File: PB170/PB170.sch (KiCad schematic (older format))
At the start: 47 parts, among them J2 USB_B_Micro, Q1 P-MOSFET-MLP_HS, SW1 SW_MEC_5E, SW2 SW_MEC_5E, U1 74HC00, U10 74HC74, U11 74HC74, U12 74HC74, U13 74HC74, U14 NE555DR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

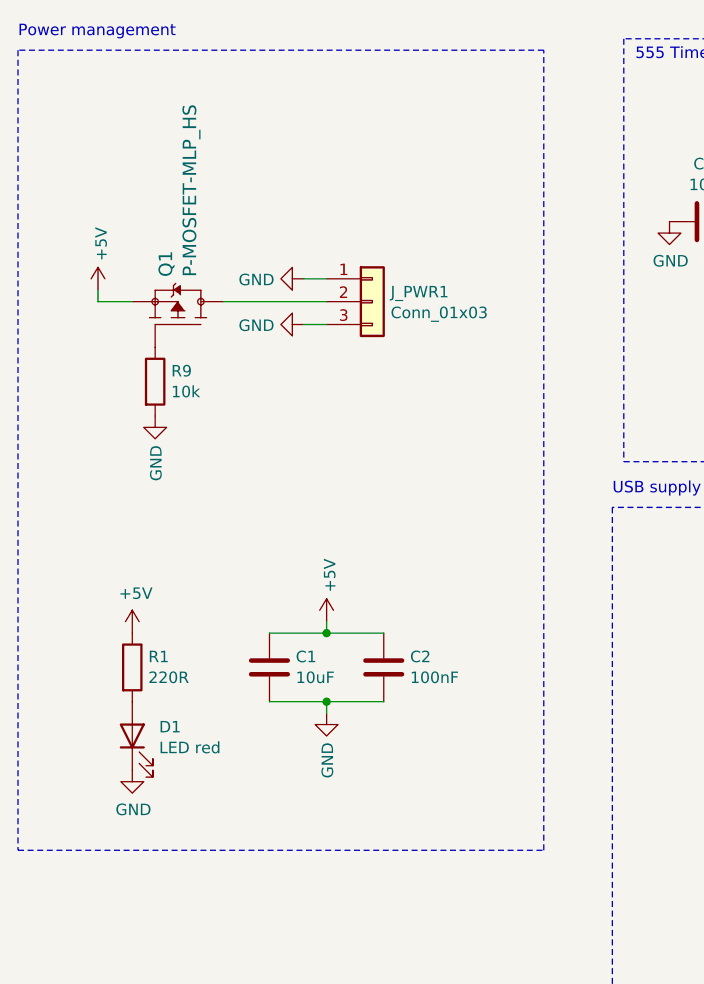
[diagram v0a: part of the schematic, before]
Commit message: Capacitors footprints added, gl & hf routing
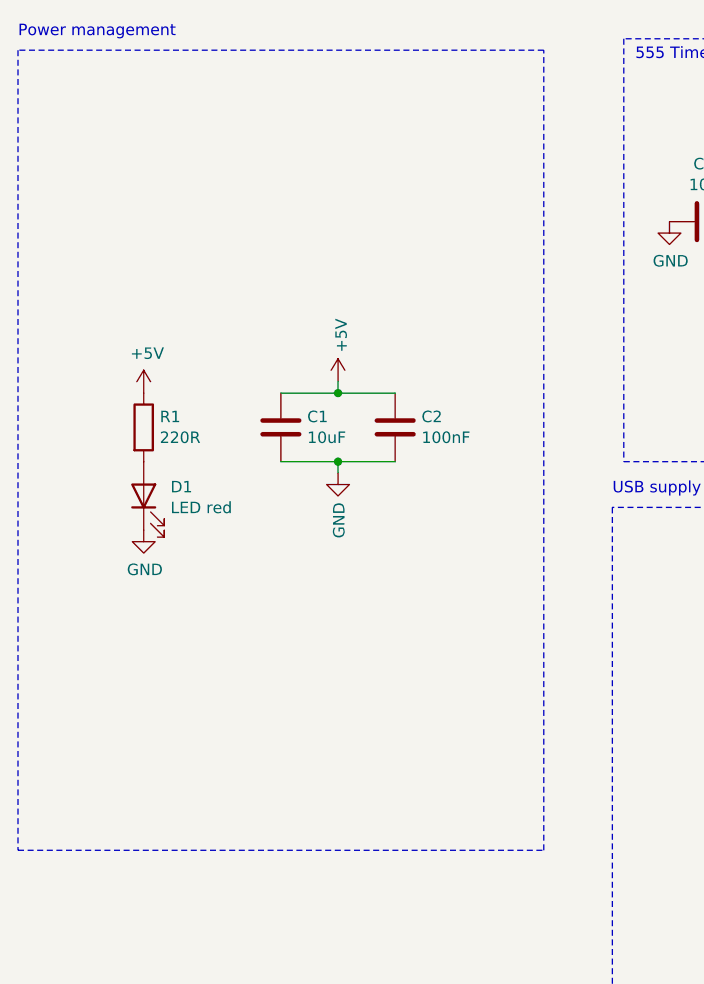
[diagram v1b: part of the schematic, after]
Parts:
- removed J_PWR1: Conn_01x03, Pin_Headers:Pin_Header_Straight_1x03_Pitch2.54mm, symbol Connector_Generic:Conn_01x03
- removed Q1: P-MOSFET-MLP_HS, PB170:MLP3.3X3.3_HS, symbol PB170:P-MOSFET-MLP_HS
- removed R9: 10k, PB170:R0603, symbol Device:R
- C2: footprint Capacitors_SMD:C_0603 -> PB170:C0603
- C3: footprint Capacitor_SMD:C_0402_1005Metric -> PB170:C0402; LCSC (none) -> C15195
- C4: footprint Capacitor_SMD:C_0805_2012Metric -> PB170:C0805; LCSC (none) -> C45783
- C5, C6: footprint Capacitors_SMD:C_0805 -> PB170:C0805
- U6: footprint Housings_SOIC:SOIC-14_3.9x8.7mm_Pitch1.27mm -> PB170:SOIC-14_L8.7-W3.9-P1.27-LS6.0-BL
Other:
- moved on the sheet: C1, C2, D1, R1

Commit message: grounded unused pins, added 3D models and photo
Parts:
- removed R2: 10k, PB170:R0603, symbol Device:R
- added RV1: R_POT, PB170:potentiometer10k, symbol Device:R_POT
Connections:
- net +5V: now also R3.1, U13.10 (~S), U13.13 (~R)
- net GND: no longer U11.6 (~Q), U11.8 (~Q), U12.6 (~Q), U12.8 (~Q), U13.10 (~S), U13.13 (~R), U13.6 (~Q), U13.8 (~Q), U13.9 (Q)
- net SET: now also U11.4 (~S)
- net at U14.7 (DIS): now also R3.2, RV1.1; no longer R3.1
- net at C4.1, U14.2 (TR), U14.6 (THR): now also RV1.2, RV1.3; no longer R3.2
- net at U9.4 (2A): now also U5.3 (1Y)
- net at U9.5 (2B): now also U5.6 (2Y)
- net at U9.6 (2Y): now also U9.12 (4A)
- no-connect marks 5 -> 12
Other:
- moved on the sheet: R3, U9B
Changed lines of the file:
@@
 Text GLabel 12000 1450 0    50   Input ~ 0
 CLOCK
-Wire Wire Line
-	12600 2700 12800 2700
-Wire Wire Line
-	12800 1550 12600 1550
 $Comp
 L power:+5V #PWR035
@@
 	1    0    0    -1
 $EndComp
-Wire Wire Line
-	12800 1550 12800 2700
 $Comp
 L power:+5V #PWR034
@@
 	-1   0    0    1
 $EndComp
-Text GLabel 12600 2500 2    50   Output ~ 0
-Q1
 Text GLabel 12000 2500 0    50   Input ~ 0
 Q0
@@
 Text GLabel 12300 4000 3    50   Input ~ 0
 SET
-Wire Wire Line
-	12800 5000 12600 5000
 $Comp
 L power:+5V #PWR038
@@
 	1    0    0    -1
 $EndComp
-Connection ~ 12800 5000
-Wire Wire Line
-	12800 3800 12600 3800
-$Comp
-L power:GND #PWR039
-U 1 1 603E70B7
-P 12800 7700
-F 0 "#PWR039" H 12800 7450 50  0001 C CNN
-F 1 "GND" H 12805 7527 50  0000 C CNN
-F 2 "" H 12800 7700 50  0001 C CNN
-F 3 "" H 12800 7700 50  0001 C CNN
-	1    12800 7700
-	1    0    0    -1
-$EndComp
-Wire Wire Line
-	12600 6050 12800 6050
 Text GLabel 12000 3700 0    50   Input ~ 0
 CLOCK
@@
 Text GLabel 12000 3600 0    50   Input ~ 0
 Q1
-Text GLabel 12600 5850 2    50   Output ~ 0
-Q4
-Text GLabel 12600 4800 2    50   Output ~ 0
-Q3
-Text GLabel 12600 3600 2    50   Output ~ 0
-Q2
 $Comp
 L 74xx:74HC74 U13
@@
 	1    0    0    -1
 $EndComp
-Wire Wire Line
-	12800 3800 12800 5000
-Connection ~ 12800 3800
-Wire Wire Line
-	12800 2700 12800 3800
-Connection ~ 12800 2700
 Wire Notes Line
 	6950 2900 8450 2900
@@
 $EndComp
 Wire Wire Line
-	5800 2000 6200 2000
+	5800 2000 6000 2000
 $Comp
 L Device:C C4
@@
 	1    0    0    -1
 $EndComp
-Wire Wire Line
-	12800 5000 12800 6050
-Wire Wire Line
-	12800 6050 12800 6600
-Connection ~ 12800 6050
-Wire Wire Line
-	12600 6950 12800 6950
-Connection ~ 12800 6950
-Wire Wire Line
-	12800 6950 12800 7150
-Wire Wire Line
-	12600 7150 12800 7150
-Wire Wire Line
-	12300 6750 12300 6600
-Wire Wire Line
-	12300 6600 12800 6600
-Connection ~ 12800 6600
-Wire Wire Line
-	12800 6600 12800 6700
-Wire Wire Line
-	12000 6950 12000 6700
-Wire Wire Line
-	12000 6700 12800 6700
-Connection ~ 12800 6700
-Wire Wire Line
-	12800 6700 12800 6950
-Wire Wire Line
-	12800 7150 12800 7450
-Connection ~ 12800 7150
-Wire Wire Line
-	12300 7350 12300 7450
-Wire Wire Line
-	12300 7450 12800 7450
-Connection ~ 12800 7450
-Wire Wire Line
-	12800 7450 12800 7550
-Wire Wire Line
-	12000 7050 12000 7550
-Wire Wire Line
-	12000 7550 12800 7550
-Connection ~ 12800 7550
-Wire Wire Line
-	12800 7550 12800 7700
 $Comp
 L PB170:74HC32 U?
@@
 L PB170:74HC32 U9
 U 2 1 603F2ABC
-P 6950 8800
-F 0 "U9" H 6925 9075 50  0000 C CNN
-F 1 "74HC32" H 6925 8984 50  0000 C CNN
-F 2 "PB170:SOIC-14_L8.7-W3.9-P1.27-LS6.0-BL" H 6400 9000 50  0001 C CNN
-F 3 "https://datasheet.lcsc.com/szlcsc/Nexperia-74HC32D-653_C5632.pdf" H 6400 9000 50  0001 C CNN
-F 4 "C5632" H 6950 8800 50  0001 C CNN "LCSC"
-	2    6950 8800
+P 6950 8750
+F 0 "U9" H 6925 9025 50  0000 C CNN
+F 1 "74HC32" H 6925 8934 50  0000 C CNN
+F 2 "PB170:SOIC-14_L8.7-W3.9-P1.27-LS6.0-BL" H 6400 8950 50  0001 C CNN
+F 3 "https://datasheet.lcsc.com/szlcsc/Nexperia-74HC32D-653_C5632.pdf" H 6400 8950 50  0001 C CNN
+F 4 "C5632" H 6950 8750 50  0001 C CNN "LCSC"
+	2    6950 8750
 	1    0    0    -1
 $EndComp
@@
 L Device:R R3
 U 1 1 602EB1DF
-P 6200 1850
-F 0 "R3" H 6270 1896 50  0000 L CNN
-F 1 "10k" H 6270 1805 50  0000 L CNN
-F 2 "PB170:R0603" V 6130 1850 50  0001 C CNN
-F 3 "https://datasheet.lcsc.com/szlcsc/Uniroyal-Elec-0603WAF1002T5E_C25804.pdf" H 6200 1850 50  0001 C CNN
-F 4 "C25804" H 6200 1850 50  0001 C CNN "LCSC"
-	1    6200 1850
-	1    0    0    -1
-$EndComp
-Connection ~ 6200 1700
-Connection ~ 6200 2000
-$Comp
-L Device:R R2
-U 1 1 602F9729
 P 6200 1550
-F 0 "R2" H 6270 1596 50  0000 L CNN
+F 0 "R3" H 6270 1596 50  0000 L CNN
 F 1 "10k" H 6270 1505 50  0000 L CNN
 F 2 "PB170:R0603" V 6130 1550 50  0001 C CNN
@@
 	1    0    0    -1
 $EndComp
+Connection ~ 6200 2000
 $Comp
 L Device:R R5
@@
 	1    0    0    -1
 $EndComp
+Text GLabel 12600 3600 2    50   Output ~ 0
+Q2
+Text GLabel 12600 4800 2    50   Output ~ 0
+Q3
+Text GLabel 12600 5850 2    50   Output ~ 0
+Q4
+Text GLabel 12600 2500 2    50   Output ~ 0
+Q1
+NoConn ~ 12600 2700
+NoConn ~ 12600 3800
+NoConn ~ 12600 5000
+NoConn ~ 12600 6050
+NoConn ~ 12600 7150
+NoConn ~ 12600 6950
+$Comp
+L power:+5V #PWR0101
+U 1 1 603E3A76
+P 12300 6750
+F 0 "#PWR0101" H 12300 6600 50  0001 C CNN
+F 1 "+5V" H 12315 6923 50  0000 C CNN
+F 2 "" H 12300 6750 50  0001 C CNN
+F 3 "" H 12300 6750 50  0001 C CNN
+	1    12300 6750
+	1    0    0    -1
+$EndComp
+$Comp
+L power:+5V #PWR0102
+U 1 1 603E3FE9
+P 12300 7350
+F 0 "#PWR0102" H 12300 7200 50  0001 C CNN
+F 1 "+5V" H 12315 7523 50  0000 C CNN
+F 2 "" H 12300 7350 50  0001 C CNN
+F 3 "" H 12300 7350 50  0001 C CNN
+	1    12300 7350
+	-1   0    0    1
+$EndComp
+$Comp
+L power:GND #PWR0103
+U 1 1 603E4B38
+P 11850 7000
+F 0 "#PWR0103" H 11850 6750 50  0001 C CNN
+F 1 "GND" H 11855 6827 50  0000 C CNN
+F 2 "" H 11850 7000 50  0001 C CNN
+F 3 "" H 11850 7000 50  0001 C CNN
+	1    11850 7000
+	1    0    0    -1
+$EndComp
+Wire Wire Line
+	11850 7000 11950 7000
+Wire Wire Line
+	11950 7000 11950 6950
+Wire Wire Line
+	11950 6950 12000 6950
+Wire Wire Line
+	11950 7000 11950 7050
+Wire Wire Line
+	11950 7050 12000 7050
+Connection ~ 11950 7000
+NoConn ~ 12600 1550
+Text GLabel 12300 1150 1    50   Input ~ 0
+SET
+$Comp
+L Device:R_POT RV1
+U 1 1 603935F3
+P 6200 1850
+F 0 "RV1" H 6131 1896 50  0000 R CNN
+F 1 "R_POT" H 6131 1805 50  0000 R CNN
+F 2 "PB170:potentiometer10k" H 6200 1850 50  0001 C CNN
+F 3 "https://datasheet.lcsc.com/szlcsc/1810170732_Nidec-Copal-Elec-ST-4EA-10K-ohm-103_C132879.pdf" H 6200 1850 50  0001 C CNN
+F 4 " C132879" H 6200 1850 50  0001 C CNN "LCSC"
+	1    6200 1850
+	1    0    0    -1
+$EndComp
+Connection ~ 6200 1700
+Wire Wire Line
+	6000 2000 6000 2600
+Wire Wire Line
+	6000 2600 6550 2600
+Wire Wire Line
+	6550 2600 6550 1850
+Wire Wire Line
+	6550 1850 6350 1850
+Connection ~ 6000 2000
+Wire Wire Line
+	6000 2000 6200 2000
 $EndSCHEMATC
